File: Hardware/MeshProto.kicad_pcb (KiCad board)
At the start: 2 copper layers, 30.2 x 31.6 mm, 103 parts, among them P1 CONN_1, P10 CONN_1, P11 CONN_1, P12 CONN_1, P13 CONN_1, P14 CONN_1, P15 CONN_1, P16 CONN_1, P17 CONN_1, P18 CONN_1, P19 CONN_1, P2 CONN_1, P20 CONN_1, P21 CONN_1, P22 CONN_1, P23 CONN_1, P24 CONN_1, P25 CONN_1, P26 CONN_1, P27 CONN_1, P28 CONN_1, P29 CONN_1, P3 CONN_1, P30 CONN_1, P31 CONN_1, P32 CONN_1, P33 CONN_1, P34 CONN_1, P35 CONN_1, P36 CONN_1, P37 CONN_1, P38 CONN_1, P39 CONN_1, P4 CONN_1, P40 CONN_1, P41 CONN_1, P42 CONN_1, P43 CONN_1, P44 CONN_1, P45 CONN_1, P46 CONN_1, P47 CONN_1, P48 CONN_1, P49 CONN_1, P5 CONN_1, P50 CONN_1, P51 CONN_1, P52 CONN_1, P53 CONN_1, P54 CONN_1, P55 CONN_1, P56 CONN_1, P57 CONN_1, P58 CONN_1, P59 CONN_1, P6 CONN_1, P60 CONN_1, P61 CONN_1, P62 CONN_1, P63 CONN_1, P64 CONN_1, P65 CONN_1, P66 CONN_1, P67 CONN_1, P68 CONN_1, P69 CONN_1, P7 CONN_1, P70 CONN_1, P71 CONN_1, P72 CONN_1, P73 CONN_1, P74 CONN_1, P75 CONN_1, P76 CONN_1, P77 CONN_1, P78 CONN_1, P79 CONN_1, P8 CONN_1, P80 CONN_1, P81 CONN_1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

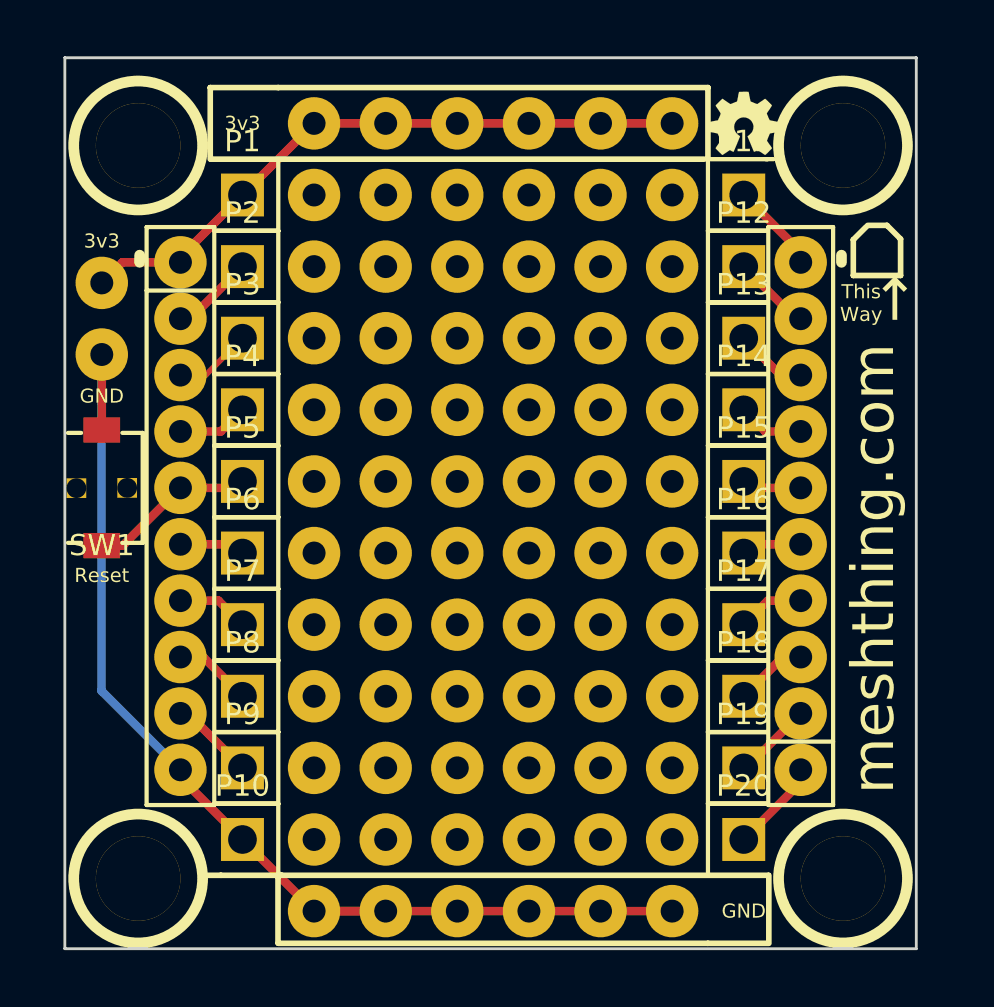
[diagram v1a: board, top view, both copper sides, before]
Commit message: Widened board by 0.5mm to fit everything better. Changed some silks.
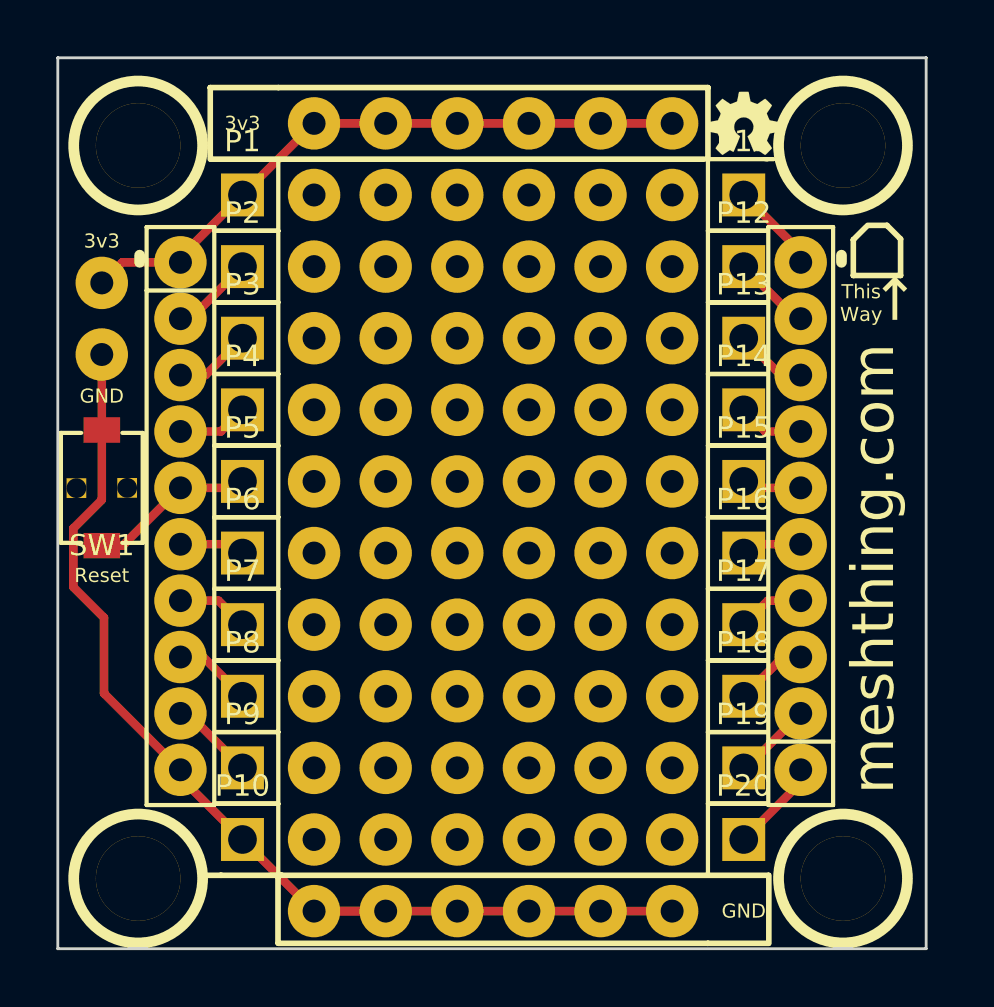
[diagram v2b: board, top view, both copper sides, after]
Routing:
- net GND: track 53.5 -> 51.6 mm
- net N-0000057: track 2.74 -> 3.63 mm
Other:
- board size 30.2 x 31.6 mm -> 30.8 x 31.6 mm
- net class Default: trace_width 0.2032 -> 0.3048
- board text added: "MeshProto v1.0 ©David Chanter Bob Powers, Andy Gelme"
- board text removed: "MeshProto v1.0 ©David Chanter, Bob Powers, Andy Gelme"
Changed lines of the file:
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@@
     (thickness 1.6)
     (drawings 33)
-    (tracks 80)
+    (tracks 84)
     (zones 0)
     (modules 103)
@@
   )
   (setup
-    (last_trace_width 0.2032)
+    (last_trace_width 0.3048)
     (user_trace_width 0.3048)
     (trace_clearance 0.2032)
@@
     (pad_drill 0.8128)
     (pad_to_mask_clearance 0.2032)
-    (aux_axis_origin 133.34 129.41)
-    (grid_origin 133.34 129.41)
+    (aux_axis_origin 133.07 129.41)
+    (grid_origin 133.07 129.41)
     (visible_elements 7FFFFF4F)
     (pcbplotparams
@@
   (net_class Default "This is the default net class."
     (clearance 0.2032)
-    (trace_width 0.2032)
+    (trace_width 0.3048)
     (via_dia 0.889)
     (via_drill 0.635)
@@
     (add_net N-0000072)
   )
+  (module _MT_TC007-TactileSwitch (layer F.Cu)
+    (at 134.71 113.004 90)
+    (fp_text reference SW1 (at -2.04 0 180) (layer F.SilkS)
+      (effects (font (size 0.75 0.75) (thickness 0.15)))
+    )
+    (fp_text value SPST (at -0.01 -2.42 90) (layer F.SilkS) hide
+      (effects (font (size 1.5 1.5) (thickness 0.15)))
+    )
+    (fp_line (start -1.95 -1.45) (end 1.95 -1.45) (layer F.SilkS) (width 0.15))
+    (fp_line (start -1.95 1.45) (end -1.95 0.73) (layer F.SilkS) (width 0.15))
+    (fp_line (start 1.95 1.45) (end 1.95 0.73) (layer F.SilkS) (width 0.15))
+    (fp_line (start -1.95 1.45) (end 1.95 1.45) (layer F.SilkS) (width 0.15))
+    (fp_line (start -1.95 -1.45) (end -1.95 -0.73) (layer F.SilkS) (width 0.15))
+    (fp_line (start 1.95 -1.45) (end 1.95 -0.73) (layer F.SilkS) (width 0.15))
+    (pad 1 smd rect (at -2.05 0 90) (size 0.9 1.3) (layers F.Cu F.Paste F.Mask)
+      (net 3 N-0000052))
+    (pad 2 smd rect (at 2.05 0 90) (size 0.9 1.3) (layers F.Cu F.Paste F.Mask)
+      (net 2 GND))
+    (pad "" thru_hole rect (at 0 0.9 90) (size 0.7 0.7) (drill 0.7) (layers *.Cu *.Mask F.SilkS))
+    (pad "" thru_hole rect (at -0.01 -0.9 90) (size 0.7 0.7) (drill 0.7) (layers *.Cu *.Mask F.SilkS))
+  )
   (module _MP_XbeeTH10Pin (layer F.Cu)
     (at 159.5 114.004 180)
@@
     (pad 10 thru_hole circle (at 0 9 180) (size 1.85928 1.85928) (drill 0.8128) (layers *.Cu *.Mask F.SilkS)
       (net 11 N-0000063))
-  )
-  (module _MT_TC007-TactileSwitch (layer F.Cu)
-    (at 134.71 113.004 90)
-    (fp_text reference SW1 (at -2.04 0 180) (layer F.SilkS)
-      (effects (font (size 0.75 0.75) (thickness 0.15)))
-    )
-    (fp_text value SPST (at -0.01 -2.42 90) (layer F.SilkS) hide
-      (effects (font (size 1.5 1.5) (thickness 0.15)))
-    )
-    (fp_line (start -1.95 1.45) (end -1.95 0.73) (layer F.SilkS) (width 0.15))
-    (fp_line (start 1.95 1.45) (end 1.95 0.73) (layer F.SilkS) (width 0.15))
-    (fp_line (start -1.95 1.45) (end 1.95 1.45) (layer F.SilkS) (width 0.15))
-    (fp_line (start -1.95 -1.2) (end -1.95 -0.73) (layer F.SilkS) (width 0.15))
-    (fp_line (start 1.95 -1.2) (end 1.95 -0.73) (layer F.SilkS) (width 0.15))
-    (pad 1 smd rect (at -2.05 0 90) (size 0.9 1.3) (layers F.Cu F.Paste F.Mask)
-      (net 3 N-0000052))
-    (pad 2 smd rect (at 2.05 0 90) (size 0.9 1.3) (layers F.Cu F.Paste F.Mask)
-      (net 2 GND))
-    (pad "" thru_hole rect (at 0 0.9 90) (size 0.7 0.7) (drill 0.7) (layers *.Cu *.Mask F.SilkS))
-    (pad "" thru_hole rect (at -0.01 -0.9 90) (size 0.7 0.7) (drill 0.7) (layers *.Cu *.Mask F.SilkS))
   )
   (module _MUSB_XBee_Board_OUTLINE_ONLY (layer F.Cu)
@@
     )
   )
-  (gr_text "OpenHardware\nUnder TAPR OHL\n tapr.org/OHL" (at 161.25 118.04 90) (layer B.SilkS)
-    (effects (font (size 0.5 0.5) (thickness 0.125)) (justify left mirror))
+  (gr_text "OpenHardware\nUnder TAPR OHL\n tapr.org/OHL" (at 161.25 116.36 90) (layer B.SilkS)
+    (effects (font (size 0.625 0.625) (thickness 0.125)) (justify left mirror))
   )
   (gr_line (start 158.25 101.345) (end 158.54 101.345) (angle 90) (layer F.SilkS) (width 0.1524))
@@
     (effects (font (size 1.5 1.5) (thickness 0.3)))
   )
-  (gr_text "MeshProto v1.0\n©David Chanter, Bob Powers,\nAndy Gelme" (at 161.25 103.66 90) (layer B.SilkS)
-    (effects (font (size 0.5 0.5) (thickness 0.1)) (justify left mirror))
+  (gr_text "MeshProto v1.0\n©David Chanter \nBob Powers, Andy Gelme" (at 161.25 103.66 90) (layer B.SilkS)
+    (effects (font (size 0.625 0.625) (thickness 0.1)) (justify left mirror))
   )
   (gr_text ↑ (at 162.8394 106.35) (layer F.SilkS)
@@
   (gr_line (start 140.97 98.806) (end 156.21 98.806) (angle 90) (layer F.SilkS) (width 0.2))
   (gr_line (start 156.083 101.346) (end 138.6 101.346) (angle 90) (layer F.SilkS) (width 0.2))
-  (gr_line (start 163.6 97.75) (end 163.6 129.35) (angle 90) (layer Edge.Cuts) (width 0.1))
-  (gr_line (start 133.4 97.75) (end 163.6 97.75) (angle 90) (layer Edge.Cuts) (width 0.1))
-  (gr_line (start 133.4 129.35) (end 133.4 97.75) (angle 90) (layer Edge.Cuts) (width 0.1))
-  (gr_line (start 163.6 129.35) (end 133.4 129.35) (angle 90) (layer Edge.Cuts) (width 0.1))
+  (gr_line (start 163.95 97.75) (end 163.95 129.35) (angle 90) (layer Edge.Cuts) (width 0.1))
+  (gr_line (start 133.15 97.75) (end 163.95 97.75) (angle 90) (layer Edge.Cuts) (width 0.1))
+  (gr_line (start 133.15 129.35) (end 133.15 97.75) (angle 90) (layer Edge.Cuts) (width 0.1))
+  (gr_line (start 163.95 129.35) (end 133.15 129.35) (angle 90) (layer Edge.Cuts) (width 0.1))
   (segment (start 137.5 105.004) (end 135.44 105.004) (width 0.3048) (layer F.Cu) (net 1))
   (segment (start 135.44 105.004) (end 134.71 105.734) (width 0.3048) (layer F.Cu) (net 1))
@@
   (segment (start 149.86 100.076) (end 152.4 100.076) (width 0.2032) (layer F.Cu) (net 1))
   (segment (start 152.4 100.076) (end 154.94 100.076) (width 0.2032) (layer F.Cu) (net 1))
+  (segment (start 133.7 115.93) (end 133.7 116.52) (width 0.3048) (layer F.Cu) (net 2))
+  (segment (start 133.7 116.52) (end 134.79 117.61) (width 0.3048) (layer F.Cu) (net 2))
+  (segment (start 134.71 110.954) (end 134.71 113.43) (width 0.3048) (layer F.Cu) (net 2) (status 400000))
+  (segment (start 133.7 114.44) (end 133.7 115.93) (width 0.3048) (layer F.Cu) (net 2))
+  (segment (start 134.71 113.43) (end 133.7 114.44) (width 0.3048) (layer F.Cu) (net 2))
+  (segment (start 137.5 123.004) (end 134.79 120.294) (width 0.3048) (layer F.Cu) (net 2) (status 400000))
+  (segment (start 134.79 120.294) (end 134.79 117.61) (width 0.3048) (layer F.Cu) (net 2))
   (segment (start 134.71 108.274) (end 134.71 110.954) (width 0.3048) (layer F.Cu) (net 2))
   (segment (start 142.24 128.016) (end 144.78 128.016) (width 0.3048) (layer F.Cu) (net 2))
-  (segment (start 134.7 109.97) (end 134.7 108.354) (width 0.3048) (layer B.Cu) (net 2))
-  (segment (start 134.7 108.354) (end 134.62 108.274) (width 0.3048) (layer B.Cu) (net 2))
-  (segment (start 134.7 120.204) (end 137.5 123.004) (width 0.3048) (layer B.Cu) (net 2))
-  (segment (start 134.7 109.97) (end 134.7 120.204) (width 0.3048) (layer B.Cu) (net 2))
   (segment (start 139.7 125.476) (end 142.24 128.016) (width 0.3048) (layer F.Cu) (net 2))
   (segment (start 142.24 128.016) (end 154.94 128.016) (width 0.3048) (layer F.Cu) (net 2))
@@
   (segment (start 138.932 111.004) (end 137.5 111.004) (width 0.3048) (layer F.Cu) (net 6))
   (segment (start 137.5 111.004) (end 138.932 111.004) (width 0.2032) (layer F.Cu) (net 6))
+  (segment (start 139.7 107.696) (end 138.392 109.004) (width 0.3048) (layer F.Cu) (net 7) (status C00000))
+  (segment (start 138.392 109.004) (end 137.5 109.004) (width 0.3048) (layer F.Cu) (net 7) (status C00000))
   (segment (start 137.5 109.004) (end 138.392 109.004) (width 0.2032) (layer F.Cu) (net 7))
-  (segment (start 138.392 109.004) (end 139.7 107.696) (width 0.2032) (layer F.Cu) (net 7))
   (segment (start 139.7 105.156) (end 137.852 107.004) (width 0.3048) (layer F.Cu) (net 8))
   (segment (start 137.852 107.004) (end 137.5 107.004) (width 0.3048) (layer F.Cu) (net 8))

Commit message: v1.1 initial changes. Increased drill size, changed libs, back silk larger.
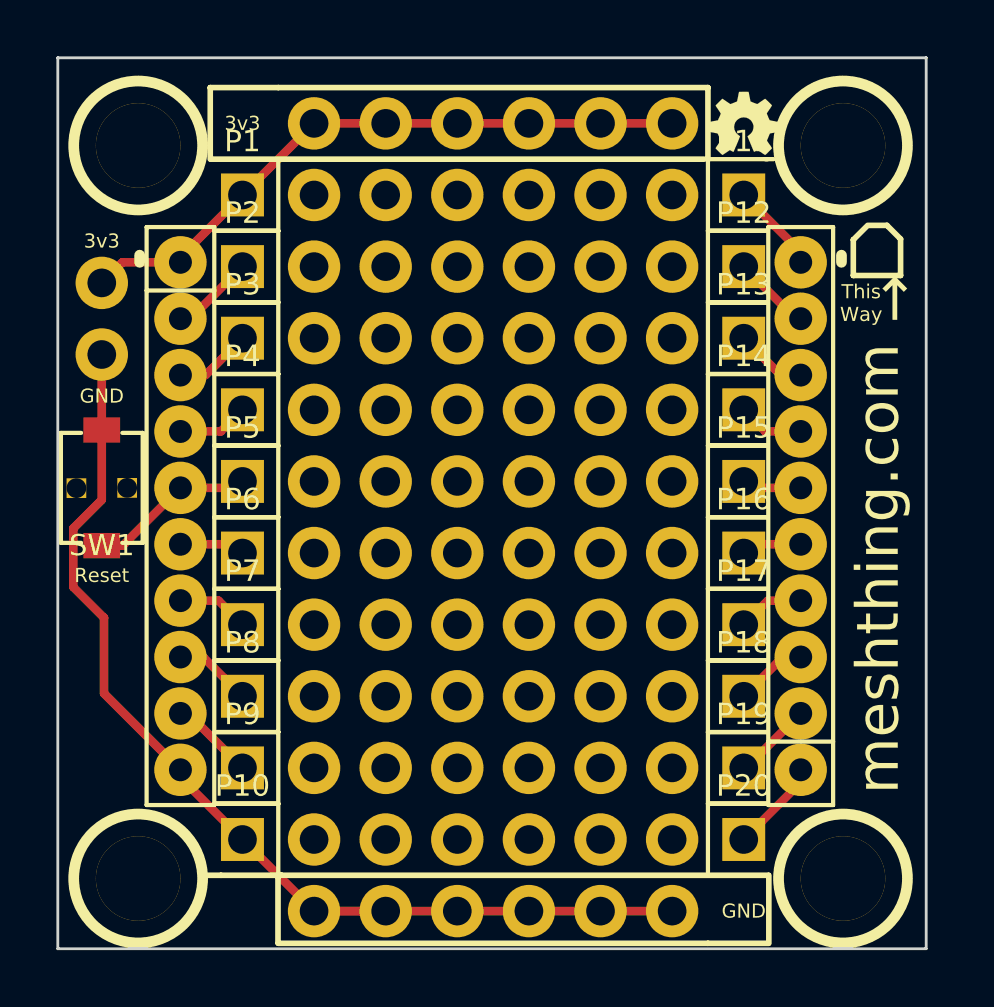
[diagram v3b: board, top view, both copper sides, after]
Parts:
- P21, P22, P23, P24, P25, P26, P27, P28, P29, P30, P31, P32, P33, P34, P35, P36, P37, P38, P39, P40, P41, P42, P43, P44, P45, P46, P47, P48, P49, P50, P51, P52, P53, P54, P55, P56, P57, P58, P59, P60, P61, P62, P63, P64, P65, P66, P67, P68, P69, P70, P71, P72, P73, P74, P75, P76, P77, P78, P79, P80, P81, P82, P83, P84, P85, P86, P87, P88, P89, P90, P91, P92, P93, P94: footprint _MP_1Pin -> _MP_:_MP_1Pin
- moved P81 0.95 mm to (134.7, 105.7)

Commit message: Bump silk version to v1.1.
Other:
- board text added: "MeshProto v1.1 ©David Chanter Bob Powers, Andy Gelme"
- board text removed: "MeshProto v1.0 ©David Chanter Bob Powers, Andy Gelme"
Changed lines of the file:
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@@
     (links 36)
     (no_connects 0)
-    (area 133.099999 97.699999 164.000001 129.400001)
+    (area 129.261801 96.5166 165.135343 130.6954)
     (thickness 1.6)
     (drawings 33)
@@
     (effects (font (size 1.5 1.5) (thickness 0.3)))
   )
-  (gr_text "MeshProto v1.0\n©David Chanter \nBob Powers, Andy Gelme" (at 162.165 103.66 90) (layer B.SilkS)
+  (gr_text "MeshProto v1.1\n©David Chanter \nBob Powers, Andy Gelme" (at 162.165 103.66 90) (layer B.SilkS)
     (effects (font (size 0.65 0.65) (thickness 0.1)) (justify left mirror))
   )

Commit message: Initial changes to v1.2.
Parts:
- removed SW1: SPST, _MT_TC007-TactileSwitch
- added P100: CONN_1, _MP_1Pin, F.Cu at (134.6, 122.9)
- added P101: CONN_1, _MP_1Pin, F.Cu at (162.6, 105.2)
- added P102: CONN_1, _MP_1Pin, F.Cu at (162.6, 107.7)
- added P103: CONN_1, _MP_1Pin, F.Cu at (162.6, 110.2)
- added P104: CONN_1, _MP_1Pin, F.Cu at (162.6, 112.8)
- added P105: CONN_1, _MP_1Pin, F.Cu at (162.6, 115.3)
- added P106: CONN_1, _MP_1Pin, F.Cu at (162.6, 117.9)
- added P107: CONN_1, _MP_1Pin, F.Cu at (162.6, 120.4)
- added P108: CONN_1, _MP_1Pin, F.Cu at (162.6, 122.9)
- added P95: CONN_1, _MP_1Pin, F.Cu at (134.6, 110.2)
- added P96: CONN_1, _MP_1Pin, F.Cu at (134.6, 112.8)
- added P97: CONN_1, _MP_1Pin, F.Cu at (134.6, 115.3)
- added P98: CONN_1, _MP_1Pin, F.Cu at (134.6, 117.9)
- added P99: CONN_1, _MP_1Pin, F.Cu at (134.6, 120.4)
- G***: moved to B.Cu
- H1, H2: footprint _MP_XbeeTH10Pin -> _MP_:_MP_XbeeTH10Pin
- moved G*** 17.8 mm to (139.7, 99.9)
- moved P82 0.58 mm to (134.6, 107.7)
- moved P81 0.58 mm to (134.6, 105.2)
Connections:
- P21 pad 1: (no net) -> Net-(P21-Pad1)
- P22 pad 1: (no net) -> Net-(P22-Pad1)
- P23 pad 1: (no net) -> Net-(P23-Pad1)
- P24 pad 1: (no net) -> Net-(P24-Pad1)
- P25 pad 1: (no net) -> Net-(P25-Pad1)
- P26 pad 1: (no net) -> Net-(P26-Pad1)
- P27 pad 1: (no net) -> Net-(P27-Pad1)
- P28 pad 1: (no net) -> Net-(P28-Pad1)
- P29 pad 1: (no net) -> Net-(P29-Pad1)
- P30 pad 1: (no net) -> Net-(P30-Pad1)
- P31 pad 1: (no net) -> Net-(P31-Pad1)
- P32 pad 1: (no net) -> Net-(P32-Pad1)
- P33 pad 1: (no net) -> Net-(P33-Pad1)
- P34 pad 1: (no net) -> Net-(P34-Pad1)
- P35 pad 1: (no net) -> Net-(P35-Pad1)
- P36 pad 1: (no net) -> Net-(P36-Pad1)
- P37 pad 1: (no net) -> Net-(P37-Pad1)
- P38 pad 1: (no net) -> Net-(P38-Pad1)
- P39 pad 1: (no net) -> Net-(P39-Pad1)
- P40 pad 1: (no net) -> Net-(P40-Pad1)
- P41 pad 1: (no net) -> Net-(P41-Pad1)
- P42 pad 1: (no net) -> Net-(P42-Pad1)
- P43 pad 1: (no net) -> Net-(P43-Pad1)
- P44 pad 1: (no net) -> Net-(P44-Pad1)
- P45 pad 1: (no net) -> Net-(P45-Pad1)
- P46 pad 1: (no net) -> Net-(P46-Pad1)
- P47 pad 1: (no net) -> Net-(P47-Pad1)
- P48 pad 1: (no net) -> Net-(P48-Pad1)
- P49 pad 1: (no net) -> Net-(P49-Pad1)
- P50 pad 1: (no net) -> Net-(P50-Pad1)
- P51 pad 1: (no net) -> Net-(P51-Pad1)
- P52 pad 1: (no net) -> Net-(P52-Pad1)
- P53 pad 1: (no net) -> Net-(P53-Pad1)
- P54 pad 1: (no net) -> Net-(P54-Pad1)
- P55 pad 1: (no net) -> Net-(P55-Pad1)
- P56 pad 1: (no net) -> Net-(P56-Pad1)
- P57 pad 1: (no net) -> Net-(P57-Pad1)
- P58 pad 1: (no net) -> Net-(P58-Pad1)
- P59 pad 1: (no net) -> Net-(P59-Pad1)
- P60 pad 1: (no net) -> Net-(P60-Pad1)
- P61 pad 1: (no net) -> Net-(P61-Pad1)
- P62 pad 1: (no net) -> Net-(P62-Pad1)
- P63 pad 1: (no net) -> Net-(P63-Pad1)
- P64 pad 1: (no net) -> Net-(P64-Pad1)
- P65 pad 1: (no net) -> Net-(P65-Pad1)
- P66 pad 1: (no net) -> Net-(P66-Pad1)
- P67 pad 1: (no net) -> Net-(P67-Pad1)
- P68 pad 1: (no net) -> Net-(P68-Pad1)
- P69 pad 1: (no net) -> Net-(P69-Pad1)
- P70 pad 1: (no net) -> Net-(P70-Pad1)
- P71 pad 1: (no net) -> Net-(P71-Pad1)
- P72 pad 1: (no net) -> Net-(P72-Pad1)
- P73 pad 1: (no net) -> Net-(P73-Pad1)
- P74 pad 1: (no net) -> Net-(P74-Pad1)
- P75 pad 1: (no net) -> Net-(P75-Pad1)
- P76 pad 1: (no net) -> Net-(P76-Pad1)
- P77 pad 1: (no net) -> Net-(P77-Pad1)
- P78 pad 1: (no net) -> Net-(P78-Pad1)
- P79 pad 1: (no net) -> Net-(P79-Pad1)
- P80 pad 1: (no net) -> Net-(P80-Pad1)
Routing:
- net Net-(H1-Pad5): track 7.91 -> 4.27 mm
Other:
- board text added: "MeshProto v1.2"
- board text added: "©M9Design.co 2013"
- board text removed: "MeshProto v1.1 ©David Chanter Bob Powers, Andy Gelme"
- board text removed: "OpenHardware Under TAPR OHL tapr.org/OHL"
- board text removed: "Reset"
- board text removed: "This Way"
- board text removed: "meshthing.com"
